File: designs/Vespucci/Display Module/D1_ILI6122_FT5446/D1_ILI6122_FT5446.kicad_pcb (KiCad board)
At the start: 4 copper layers, 42.6 x 30 mm, 61 parts, among them J1 PCIExpress, J2 FFC_ILI6122, J3 FFC_FT5446, Q2 BSS138W, Q3 BSS138W, SW1 SW_Push, U1 NC7WZ14, U2 NC7WZ14, U3 TPS61165DRV, U4 SST39VF3201C-70-4I-B3KE, U5 STM32F429IGTx

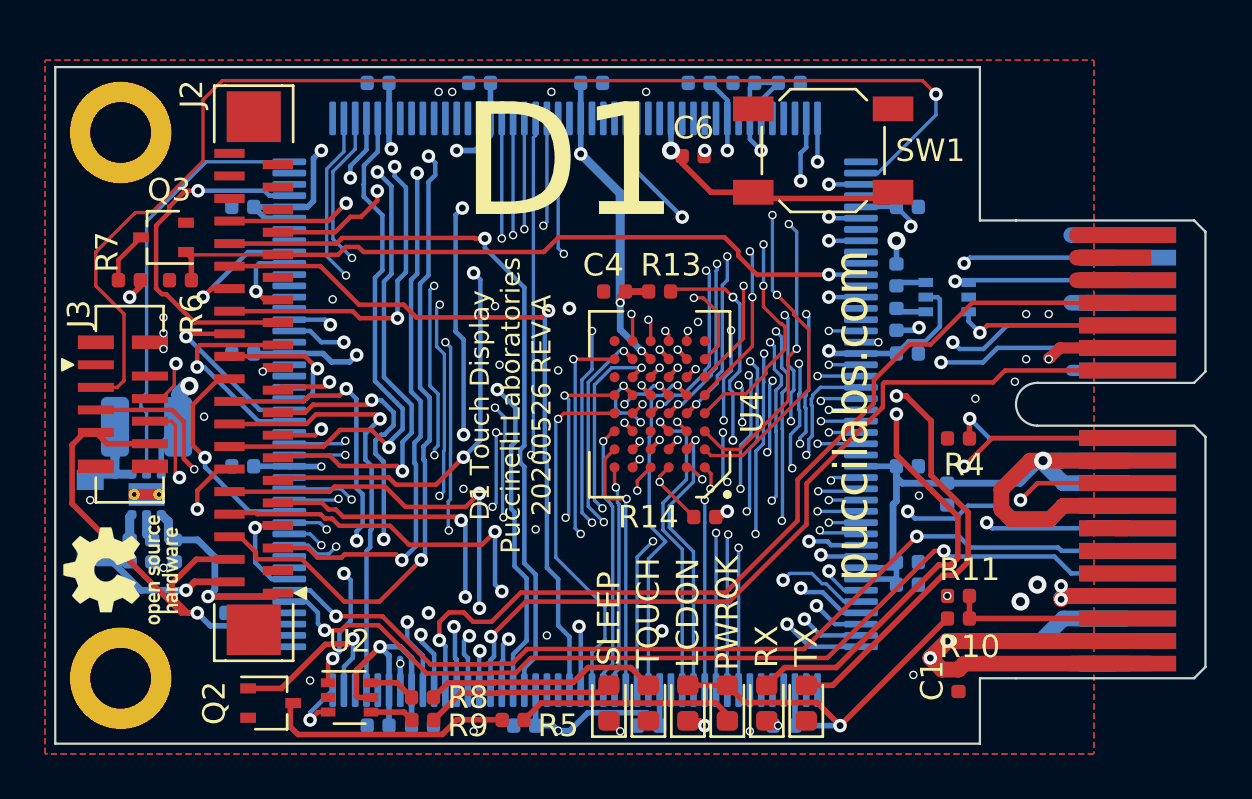
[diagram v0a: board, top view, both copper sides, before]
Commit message: Ordered: D1 Rev A, R1 Rev B, P1 Rev B
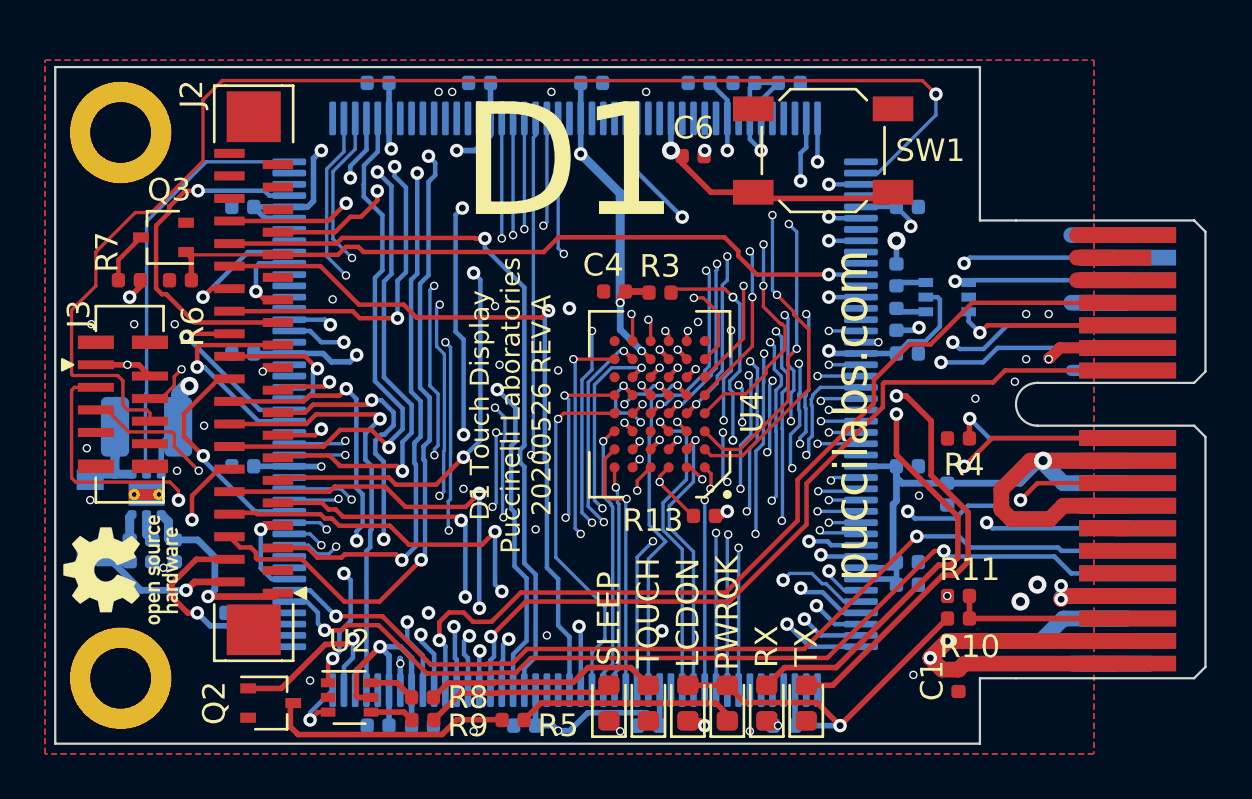
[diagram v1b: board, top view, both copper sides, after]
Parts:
- removed R14: 39K, Resistor_SMD:R_0402_1005Metric
- added R3: 39K, Resistor_SMD:R_0402_1005Metric, F.Cu at (151.5, 95.8)
- moved R13 10.1 mm to (153.5, 105.7), turned to 180 degrees
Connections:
- J2 pad GND: GND -> (no net)
- J3 pad 1: GND -> +3V3
- J3 pad 2: GND -> +3V3
- J3 pad 3: /D1_DisplayInterface/~TP_RST -> /D1_STM32F429/I2C_SCL
- J3 pad 4: /~TP_INT -> /D1_STM32F429/I2C_SDA
- J3 pad 5: /D1_STM32F429/I2C_SDA -> /~TP_INT
- J3 pad 6: /D1_STM32F429/I2C_SCL -> /D1_DisplayInterface/~TP_RST
- J3 pad 7: +3V3 -> GND
- J3 pad 8: +3V3 -> GND
- R13 pad 2: Net-(R13-Pad2) -> /D1_STM32F429/FMC_nWAIT
- U3 pad 7: GND -> (no net)
- U4 pad B3: Net-(R13-Pad2) -> Net-(R3-Pad2)
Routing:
- net Net-(R3-Pad2): track 0.00 -> 13.0 mm, vias 0 -> 3
- net Net-(R13-Pad2): track 13.0 -> 0.00 mm, vias 3 -> 0
- net /D1_STM32F429/I2C_SCL: track 37.2 -> 43.5 mm
- net /D1_DisplayInterface/~TP_RST: track 55.1 -> 58.6 mm
- net +3V3: track 304.1 -> 301.4 mm, vias 20 -> 21
- net /D1_STM32F429/I2C_SDA: track 39.5 -> 40.8 mm
- net /~TP_INT: track 44.7 -> 43.8 mm
- net /D1_DisplayInterface/LCD_R7: track 24.7 -> 25.3 mm
- net GND: vias 41 -> 43
